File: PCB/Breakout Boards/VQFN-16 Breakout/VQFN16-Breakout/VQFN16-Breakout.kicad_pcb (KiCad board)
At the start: 2 copper layers, 10.7 x 20.8 mm, 3 parts, among them J1 Conn_01x08_Pin, J2 Conn_01x08_Pin

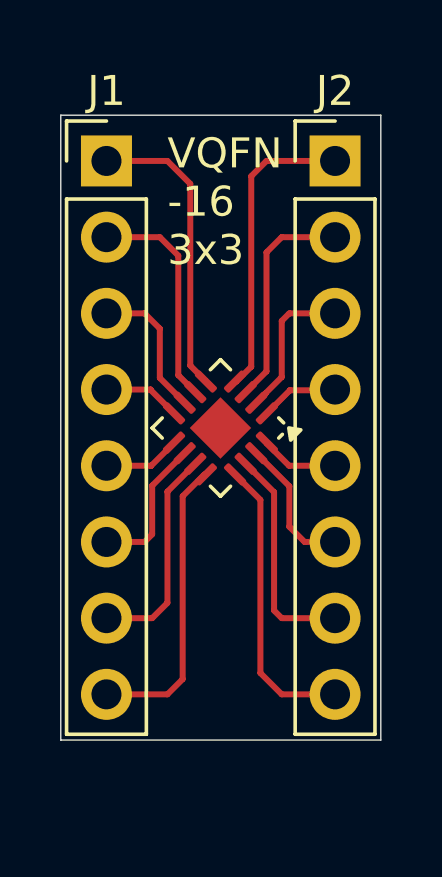
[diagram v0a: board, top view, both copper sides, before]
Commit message: VQFN16
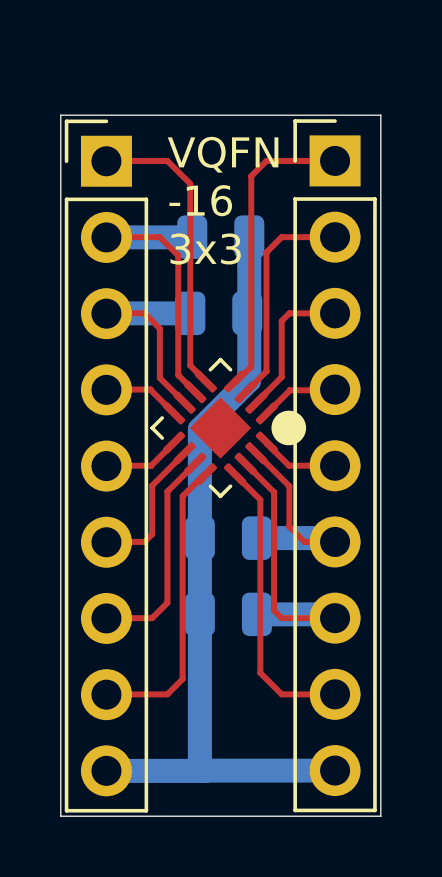
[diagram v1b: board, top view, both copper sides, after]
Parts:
- removed J1: Conn_01x08_Pin, Connector_PinHeader_2.54mm:PinHeader_1x08_P2.54mm_Vertical
- added C1: 100nF, Capacitor_SMD:C_0805_2012Metric, B.Cu at (120.6, 68.6)
- added C2: 100nF, Capacitor_SMD:C_0805_2012Metric, B.Cu at (120.9, 78.6)
- added C3: 100nF, Capacitor_SMD:C_0805_2012Metric, B.Cu at (120.7, 66.0)
- added C4: 100nF, Capacitor_SMD:C_0805_2012Metric, B.Cu at (120.9, 76.1)
- added J3: Conn_01x09_Pin, Connector_PinHeader_2.54mm:PinHeader_1x09_P2.54mm_Vertical, F.Cu at (124.5, 63.5)
- J2: value Conn_01x08_Pin -> Conn_01x09_Pin; footprint Connector_PinHeader_2.54mm:PinHeader_1x08_P2.54mm_Vertical -> Connector_PinHeader_2.54mm:PinHeader_1x09_P2.54mm_Vertical
- moved J2 7.62 mm to (116.8, 63.5)
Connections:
- U1 pad 1: Net-(J2-Pin_4) -> Net-(J3-Pin_4)
- U1 pad 10: Net-(J1-Pin_6) -> Net-(J2-Pin_6)
- U1 pad 11: Net-(J1-Pin_7) -> Net-(J2-Pin_7)
- U1 pad 12: Net-(J1-Pin_8) -> Net-(J2-Pin_8)
- U1 pad 13: Net-(J2-Pin_8) -> Net-(J3-Pin_8)
- U1 pad 14: Net-(J2-Pin_7) -> Net-(J3-Pin_7)
- U1 pad 15: Net-(J2-Pin_6) -> Net-(J3-Pin_6)
- U1 pad 16: Net-(J2-Pin_5) -> Net-(J3-Pin_5)
- U1 pad 2: Net-(J2-Pin_3) -> Net-(J3-Pin_3)
- U1 pad 3: Net-(J2-Pin_2) -> Net-(J3-Pin_2)
- U1 pad 4: Net-(J2-Pin_1) -> Net-(J3-Pin_1)
- U1 pad 5: Net-(J1-Pin_1) -> Net-(J2-Pin_1)
- U1 pad 6: Net-(J1-Pin_2) -> Net-(J2-Pin_2)
- U1 pad 7: Net-(J1-Pin_3) -> Net-(J2-Pin_3)
- U1 pad 8: Net-(J1-Pin_4) -> Net-(J2-Pin_4)
- U1 pad 9: Net-(J1-Pin_5) -> Net-(J2-Pin_5)
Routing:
- net GND: track 0.00 -> 25.8 mm
- net Net-(J3-Pin_1): track 0.00 -> 10.1 mm
- net Net-(J3-Pin_7): track 0.00 -> 10.1 mm
- net Net-(J1-Pin_8): track 9.92 -> 0.00 mm
- net Net-(J1-Pin_1): track 9.92 -> 0.00 mm
- net Net-(J3-Pin_8): track 0.00 -> 9.75 mm
- net Net-(J3-Pin_2): track 0.00 -> 7.44 mm
- net Net-(J1-Pin_2): track 7.44 -> 0.00 mm
- net Net-(J3-Pin_6): track 0.00 -> 7.30 mm
- net Net-(J1-Pin_7): track 7.26 -> 0.00 mm
- net Net-(J3-Pin_3): track 0.00 -> 4.96 mm
- net Net-(J1-Pin_3): track 4.80 -> 0.00 mm
- net Net-(J1-Pin_6): track 4.78 -> 0.00 mm
- net Net-(J2-Pin_2): track 7.44 -> 10.3 mm
- net Net-(J2-Pin_3): track 4.96 -> 7.60 mm
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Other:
- board size 10.7 x 20.8 mm -> 10.7 x 23.4 mm
